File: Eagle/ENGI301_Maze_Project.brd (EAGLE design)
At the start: 135.9 x 63.5 mm, 27 parts, among them U3 MOD-LED8X8RGB-CONN, U4 MOD-LED8X8RGB-CONN, U5 CEM-1203, U7 POCKETBEAGLE

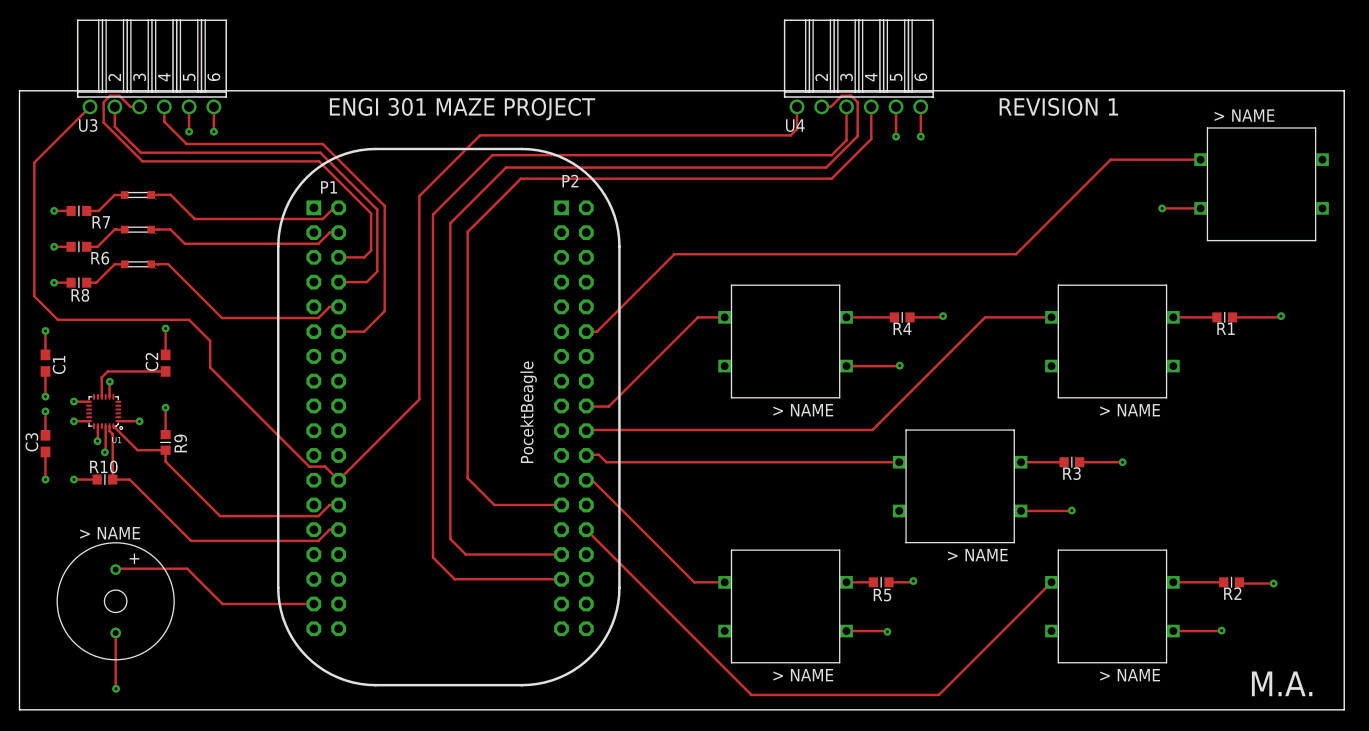
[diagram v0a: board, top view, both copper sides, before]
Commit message: Maze Project Eagle Board
-Properly connected 5 volt pins
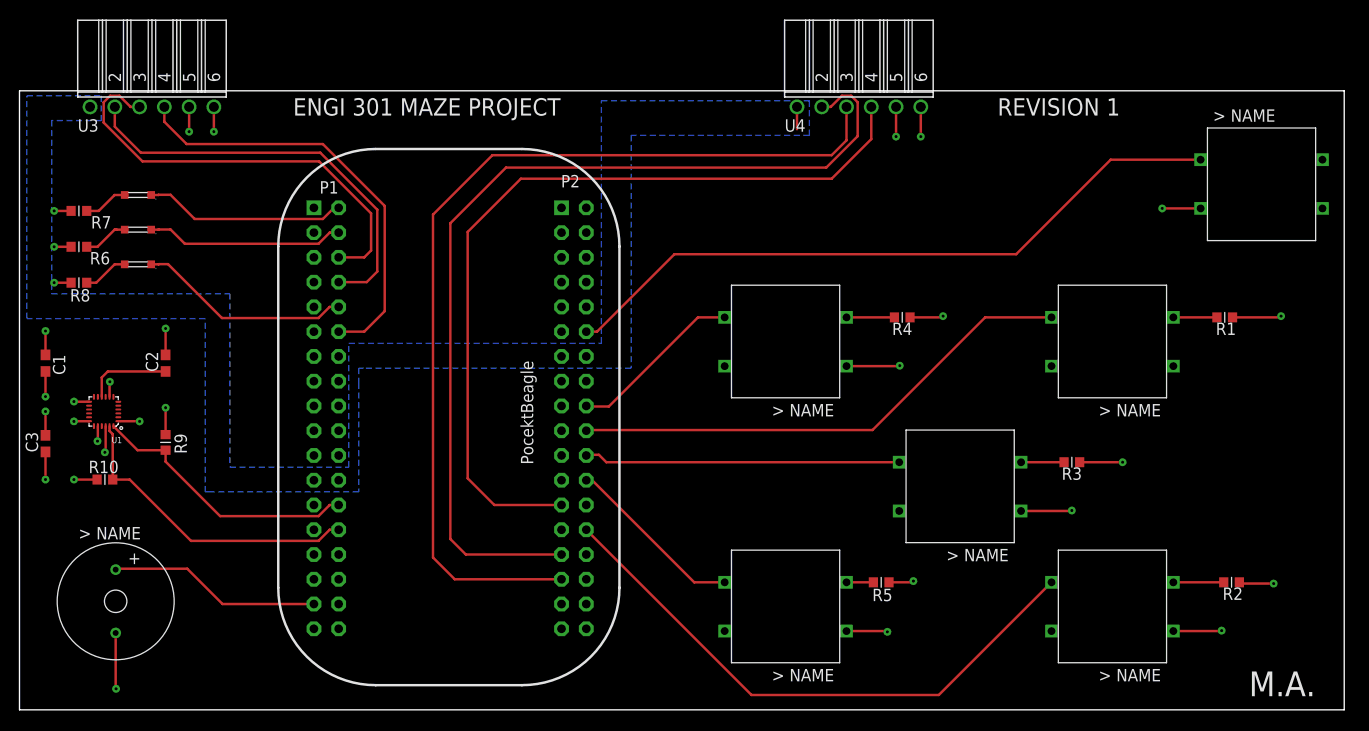
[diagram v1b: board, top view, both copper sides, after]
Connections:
- removed net SYS_VDD2_5V: U7.49
- net SYS_VDD1_5V: now also U7.49
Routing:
- net SYS_VDD1_5V: track 138.9 -> 2.29 mm
- added copper zone on layer 16, net SYS_VDD1_5V
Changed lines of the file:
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@@
 <setting verticaltext="up"/>
 </settings>
-<grid distance="5" unitdist="mil" unit="mil" style="lines" multiple="1" display="yes" altdistance="5" altunitdist="mil" altunit="mil"/>
+<grid distance="20" unitdist="mil" unit="mil" style="lines" multiple="1" display="yes" altdistance="5" altunitdist="mil" altunit="mil"/>
 <layers>
 <layer number="1" name="Top" color="4" fill="1" visible="yes" active="yes"/>
@@
 <wire x1="160.02" y1="63.5" x2="24.13" y2="63.5" width="0" layer="20"/>
 <wire x1="24.13" y1="63.5" x2="24.13" y2="0" width="0" layer="20"/>
-<text x="55.753" y="60.96" size="1.778" layer="25">ENGI 301 MAZE PROJECT</text>
+<text x="52.197" y="60.96" size="1.778" layer="25">ENGI 301 MAZE PROJECT</text>
 <text x="124.46" y="60.96" size="1.778" layer="25">REVISION 1</text>
 <text x="150.241" y="1.397" size="2.54" layer="25">M.A.</text>
@@
 <contactref element="U4" pad="1"/>
 <contactref element="U7" pad="24"/>
-<wire x1="56.87" y1="23.554" x2="55.473" y2="24.951" width="0.254" layer="1"/>
-<wire x1="55.473" y1="24.951" x2="53.85655" y2="24.951" width="0.254" layer="1"/>
-<wire x1="53.85655" y1="24.951" x2="43.688" y2="35.11955" width="0.254" layer="1"/>
-<wire x1="43.688" y1="35.11955" x2="43.688" y2="37.846" width="0.254" layer="1"/>
-<wire x1="43.688" y1="37.846" x2="41.529" y2="40.005" width="0.254" layer="1"/>
-<wire x1="28.067" y1="40.005" x2="25.654" y2="42.418" width="0.254" layer="1"/>
-<wire x1="25.654" y1="42.418" x2="25.654" y2="56.134" width="0.254" layer="1"/>
-<wire x1="25.654" y1="56.134" x2="31.369" y2="61.849" width="0.254" layer="1"/>
-<wire x1="41.529" y1="40.005" x2="28.067" y2="40.005" width="0.254" layer="1"/>
-<wire x1="56.87" y1="23.554" x2="65.151" y2="31.835" width="0.254" layer="1"/>
-<wire x1="65.151" y1="31.835" x2="65.151" y2="52.705" width="0.254" layer="1"/>
-<wire x1="65.151" y1="52.705" x2="71.374" y2="58.928" width="0.254" layer="1"/>
 <wire x1="103.886" y1="59.563" x2="103.886" y2="61.849" width="0.254" layer="1"/>
-<wire x1="71.374" y1="58.928" x2="103.251" y2="58.928" width="0.254" layer="1"/>
-<wire x1="103.251" y1="58.928" x2="103.886" y2="59.563" width="0.254" layer="1"/>
-</signal>
-<signal name="SYS_VDD2_5V">
 <contactref element="U7" pad="49"/>
+<polygon width="0.254" layer="16">
+<vertex x="102.616" y="62.484"/>
+<vertex x="105.156" y="62.484"/>
+<vertex x="105.156" y="58.928"/>
+<vertex x="86.868" y="58.928"/>
+<vertex x="86.868" y="35.052"/>
+<vertex x="59.436" y="35.052"/>
+<vertex x="58.928" y="35.052"/>
+<vertex x="58.928" y="33.528"/>
+<vertex x="58.928" y="22.352"/>
+<vertex x="43.688" y="22.352"/>
+<vertex x="43.18" y="22.352"/>
+<vertex x="43.18" y="40.132"/>
+<vertex x="24.892" y="40.132"/>
+<vertex x="24.892" y="41.148"/>
+<vertex x="24.892" y="62.992"/>
+<vertex x="32.512" y="62.992"/>
+<vertex x="32.512" y="60.452"/>
+<vertex x="27.432" y="60.452"/>
+<vertex x="27.432" y="42.672"/>
+<vertex x="45.72" y="42.672"/>
+<vertex x="45.72" y="24.892"/>
+<vertex x="57.912" y="24.892"/>
+<vertex x="57.912" y="37.592"/>
+<vertex x="83.82" y="37.592"/>
+<vertex x="83.82" y="62.484"/>
+</polygon>
 </signal>
 </signals>
